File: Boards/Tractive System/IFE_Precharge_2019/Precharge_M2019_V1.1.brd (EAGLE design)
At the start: 33 x 39.4 mm, 20 parts

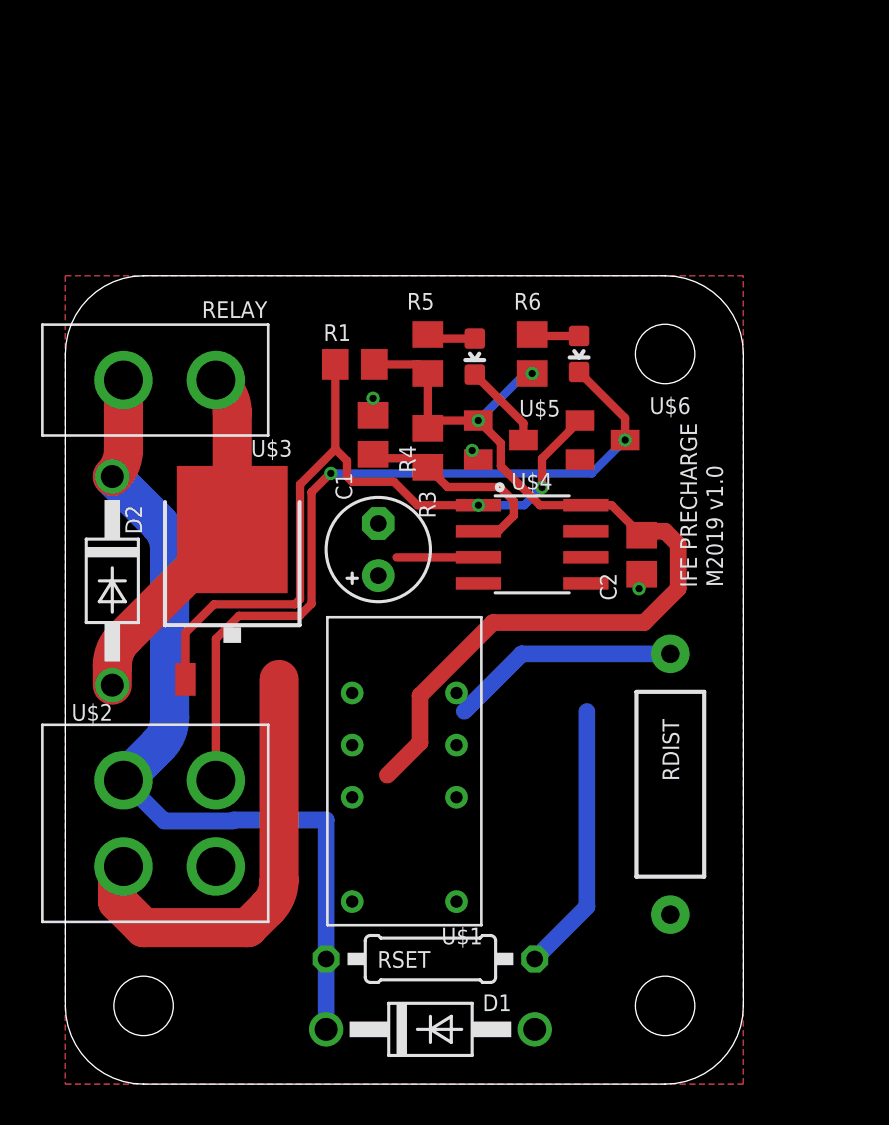
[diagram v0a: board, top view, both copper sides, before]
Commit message: Precharge 1.2 finished, added .gitignore
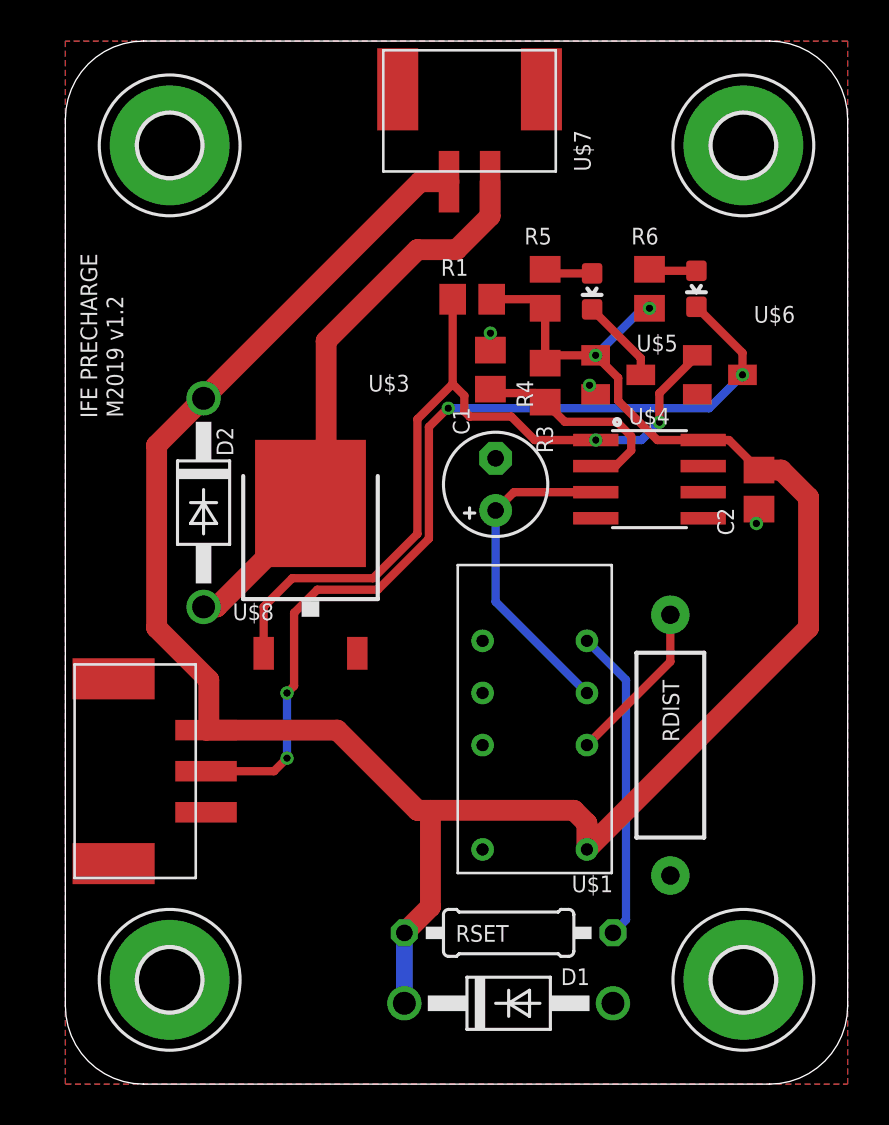
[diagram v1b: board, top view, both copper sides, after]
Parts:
- removed RELAY: MINIFIT_JR_5566-02, Display_Custom:MINIFIT_JR_5566-02
- removed U$2: MINIFIT_JR_5566-04, Display_Custom:MINIFIT_JR_5566-04
- added H1, H2, H3, H4: MOUNT-PAD-ROUND3.0, holes:3,0-PAD
- added U$7: 505575-02, MOLEX:505575-02
- added U$8: 505575-03, MOLEX:505575-03
- moved U$1 6.84 mm to (22.9, 17.8)
- moved PRECHARGE 6.54 mm to (30.7, 38.7)
- moved R4 6.54 mm to (20.7, 34.8)
- moved C1 6.54 mm to (21.0, 29.2)
- moved R1 6.54 mm to (19.8, 38.2)
- moved AIR_ON 6.54 mm to (25.7, 38.6)
- moved R3 6.54 mm to (23.4, 34.2)
- moved R5 6.54 mm to (23.4, 38.7)
- moved R6 6.54 mm to (28.4, 38.7)
- moved U$4 6.54 mm to (28.4, 29.5)
- moved U$5 6.54 mm to (26.9, 34.5)
- moved U$6 6.54 mm to (31.9, 34.5)
- moved C2 6.54 mm to (33.8, 29.0)
- moved D2 5.85 mm to (6.73, 28.3)
- moved U$3 4.02 mm to (11.9, 25.8)
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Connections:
- removed net N$4: D2.A, RELAY.1, U$3.2
- new net RELAY-: D2.A, U$3.2, U$7.2
- net GND: now also H1.B3,0, H2.B3,0, H3.B3,0, H4.B3,0, U$8.1; no longer U$2.4
- net PRECHARGE_COMPLETE: now also U$8.2; no longer U$2.1
- net V+: now also U$7.1, U$8.3; no longer RELAY.2, U$2.3
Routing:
- net RELAY-: track 0.00 -> 28.9 mm
- net V+: track 88.5 -> 113.3 mm
- net GND: track 22.0 -> 0.75 mm
- net N$4: track 17.4 -> 0.00 mm
- net TIMING: track 3.99 -> 16.0 mm
- net PRECHARGE_COMPLETE: track 38.3 -> 45.5 mm, vias 2 -> 4
- net N$3: track 11.2 -> 8.03 mm
- net PRECHARGE: track 36.7 -> 39.4 mm
- net N$1: track 13.1 -> 15.3 mm
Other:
- board size 33 x 39.4 mm -> 38.1 x 50.8 mm
- board text added: "M2019 v1.2"
- board text removed: "M2019 v1.0"
